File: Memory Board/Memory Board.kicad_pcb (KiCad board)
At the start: 4 copper layers, 50.8 x 50.8 mm, 40 parts, among them IC1 W25Q01JVZEIQ, IC2 MCP2557FDT-H_MNY, J1 USB4056-03-A_REVA2, J2 Conn_01x04_Socket, J3 Conn_01x04_Socket, J4 Conn_01x04_Socket, SW1 SW_SPST, U1 STM32G473CBTx, U2 LD1117S33TR_SOT223, U3 LD1117S50TR_SOT223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

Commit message: Layout work
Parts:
- added J5: Conn_01x02_Socket, Connector_PinHeader_2.54mm:PinHeader_1x02_P2.54mm_Vertical, F.Cu at (27.4, 37.2)
- J4: value Conn_01x04_Socket -> Conn_01x02_Socket; footprint Connector_PinHeader_2.54mm:PinHeader_1x04_P2.54mm_Vertical -> Connector_PinHeader_2.54mm:PinHeader_1x02_P2.54mm_Vertical
- moved C1 39.5 mm to (80.2, 35.5)
- moved C6 39.5 mm to (77.9, 35.1)
- moved C7 39.5 mm to (80.2, 32.6)
- moved C5 39.5 mm to (79.1, 34.6)
- moved C8 39.5 mm to (78.9, 32.1)
- moved D1 33.4 mm to (60.4, 53.0), turned to 180 degrees
- moved R2 30.9 mm to (57.3, 53.0), turned to 0 degrees
- moved C10 20.5 mm to (31.9, 49.7), turned to 90 degrees
- moved R3 19.8 mm to (39.5, 39.0), turned to -135 degrees
- moved R4 18.9 mm to (40.6, 40.1), turned to -135 degrees
- moved U2 18.1 mm to (37.1, 51.9), turned to 180 degrees
- moved R7 18.0 mm to (41.7, 41.2), turned to 45 degrees
- moved C11 17.5 mm to (44.4, 53.5), turned to 0 degrees
- moved C2 17.2 mm to (44.3, 41.7), turned to 90 degrees
- moved J1 17.1 mm to (49.5, 61.6)
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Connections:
- J4 pad 1: SYS_SWDIO -> SYS_SWCLK
- J4 pad 2: GND -> SYS_SWDIO
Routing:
- net GND: track 7.65 -> 22.8 mm, vias 4 -> 18
- net PWR IN: track 0.00 -> 7.37 mm
- net +5V: track 0.00 -> 6.94 mm
- net +3.3V: track 4.29 -> 9.08 mm, vias 1 -> 7
- net RCC_OCC_IN: track 0.00 -> 4.78 mm
- net SYS_SWCLK: track 0.00 -> 3.91 mm
- net SYS_SWDIO: track 0.00 -> 3.66 mm
- net RCC_OCC_OUT: track 0.00 -> 2.98 mm
- net Net-(D1-A): track 0.00 -> 1.46 mm
- added copper zone on F.Cu, net +3.3V
- added copper zone on F.Cu, net +5V
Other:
- board size 50.8 x 50.8 mm -> 38.1 x 38.1 mm
- board text added: "+3.3V"
- board text added: "3.3V REG"
- board text added: "5V REG"
- board text added: "CLK"
- board text added: "DIO"
- board text added: "GND"
- board text added: "PWR IN"
- board text added: "PWR ON"

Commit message: Lab Work
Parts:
- removed C11: .1uF, Capacitor_SMD:C_0402_1005Metric
- removed C12: 10uF, Capacitor_SMD:C_0603_1608Metric
- removed J5: Conn_01x02_Socket, Connector_PinHeader_2.54mm:PinHeader_1x02_P2.54mm_Vertical
- removed U3: LD1117S50TR_SOT223, Package_TO_SOT_SMD:SOT-223-3_TabPin2
- J4: value Conn_01x02_Socket -> Conn_01x04_Socket; footprint Connector_PinHeader_2.54mm:PinHeader_1x02_P2.54mm_Vertical -> Connector_PinHeader_2.54mm:PinHeader_1x04_P2.54mm_Vertical
- R3, R4, R7: footprint Resistor_SMD:R_0603_1608Metric -> Resistor_SMD:R_0402_1005Metric
- U1: moved to B.Cu
- moved C7 41.2 mm to (40.3, 43.4)
- moved C1 41.1 mm to (40.3, 45.8)
- moved C5 41.1 mm to (39.3, 44.9)
- moved C6 41.1 mm to (38.0, 45.4)
- moved C8 41.1 mm to (39.1, 42.4)
- moved D1 33.9 mm to (30.7, 36.5)
- moved R2 33.9 mm to (27.7, 36.5)
- moved J3 25.0 mm to (43.1, 62.0), turned to -90 degrees
- moved LED1 25.0 mm to (58.7, 51.0)
- moved C10 19.8 mm to (51.6, 47.6)
- moved IC2 19.8 mm to (34.6, 41.8), turned to 180 degrees
- moved R3 19.3 mm to (53.9, 51.8), turned to 0 degrees
- moved J4 17.3 mm to (43.1, 59.1)
- moved R4 16.4 mm to (53.9, 49.8), turned to 0 degrees
- moved R7 15.5 mm to (53.9, 50.8), turned to 180 degrees
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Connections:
- C15 pad 1: +5V -> PWR IN
- IC2 pad 3: +5V -> PWR IN
- J4 pad 1: SYS_SWCLK -> SYS_SWDIO
- J4 pad 2: SYS_SWDIO -> SYS_SWCLK
- U1 pad 25: unconnected-(U1-PB11-Pad25) -> LED_R
- U1 pad 27: unconnected-(U1-PB13-Pad27) -> LED_B
- U1 pad 29: unconnected-(U1-PB15-Pad29) -> LED_G
- U1 pad 30: LED_R -> unconnected-(U1-PA8-Pad30)
- U1 pad 31: LED_G -> unconnected-(U1-PA9-Pad31)
- U1 pad 32: LED_B -> unconnected-(U1-PA10-Pad32)
- U1 pad 39: TXD -> unconnected-(U1-PA15-Pad39)
- U1 pad 41: unconnected-(U1-PB4-Pad41) -> TXD
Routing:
- net GND: track 22.8 -> 0.00 mm, vias 18 -> 0
- net CAN_FD_H: track 15.1 -> 0.00 mm, vias 1 -> 0
- net CAN_FD_L: track 14.5 -> 0.00 mm, vias 2 -> 0
- net +3.3V: track 9.08 -> 0.00 mm, vias 7 -> 0
- net PWR IN: track 7.37 -> 0.00 mm
- net +5V: track 6.94 -> 0.00 mm
- net RCC_OCC_IN: track 4.78 -> 0.00 mm
- net SYS_SWCLK: track 3.91 -> 0.00 mm
- net SYS_SWDIO: track 3.66 -> 0.00 mm
- net Net-(C16-Pad2): track 3.28 -> 0.00 mm
- net RCC_OCC_OUT: track 2.98 -> 0.00 mm
- net Net-(SW1-B): track 2.22 -> 0.00 mm, vias 1 -> 0
- net Net-(D1-A): track 1.46 -> 0.00 mm
- removed copper zone on F.Cu, net +5V
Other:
- board text removed: "+3.3V"
- board text removed: "5V REG"
- board text removed: "GND"
- board text removed: "PWR IN"

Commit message: No work donw
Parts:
- moved C14 1.96 mm to (46.6, 37.4), turned to 0 degrees
- moved C13 1.86 mm to (44.7, 37.4), turned to 180 degrees
- moved D1 1.14 mm to (31.9, 36.6)
- moved R2 1.14 mm to (28.8, 36.6)
- moved X1 0.13 mm to (45.7, 35.4), turned to 90 degrees
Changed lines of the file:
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@@
   (net 64 "unconnected-(U1-PA10-Pad32)")
   (footprint "Capacitor_SMD:C_0402_1005Metric" (layer "F.Cu")
-    (at 46.546 37.3844)
+    (at 44.69 37.35 180)
     (descr "Capacitor SMD 0402 (1005 Metric), square (rectangular) end terminal, IPC_7351 nominal, (Body size source: IPC-SM-782 page 76, https://www.pcb-3d.com/wordpress/wp-content/uploads/ipc-sm-782a_amendment_1_and_2.pdf), generated with kicad-footprint-generator")
     (tags "capacitor")
@@
     (property "ki_keywords" "cap capacitor")
     (attr smd)
-    (fp_text reference "C13" (at 1.3522 -0.7942) (layer "F.SilkS")
+    (fp_text reference "C13" (at 1.46 0.82) (layer "F.SilkS")
         (effects (font (size 0.5 0.5) (thickness 0.1) bold))
     )
@@
     (fp_line (start 0.5 0.25) (end -0.5 0.25)
       (stroke (width 0.1) (type solid)) (layer "F.Fab"))
-    (pad "1" smd roundrect (at -0.48 0) (size 0.56 0.62) (layers "F.Cu" "F.Paste" "F.Mask") (roundrect_rratio 0.25)
+    (pad "1" smd roundrect (at -0.48 0 180) (size 0.56 0.62) (layers "F.Cu" "F.Paste" "F.Mask") (roundrect_rratio 0.25)
       (net 4 "RCC_OCC_IN") (pintype "passive"))
-    (pad "2" smd roundrect (at 0.48 0) (size 0.56 0.62) (layers "F.Cu" "F.Paste" "F.Mask") (roundrect_rratio 0.25)
+    (pad "2" smd roundrect (at 0.48 0 180) (size 0.56 0.62) (layers "F.Cu" "F.Paste" "F.Mask") (roundrect_rratio 0.25)
       (net 2 "GND") (pintype "passive"))
     (model "${KICAD6_3DMODEL_DIR}/Capacitor_SMD.3dshapes/C_0402_1005Metric.wrl"
@@
     (property "ki_keywords" "cap capacitor")
     (attr smd)
-    (fp_text reference "C2" (at 0 0 90) (layer "F.SilkS")
+    (fp_text reference "C2" (at 0.01 0.02 90) (layer "F.SilkS")
         (effects (font (size 0.25 0.25) (thickness 0.05) bold))
     )
@@
   )
   (footprint "Oscillator:Oscillator_SMD_ECS_2520MV-xxx-xx-4Pin_2.5x2.0mm" (layer "F.Cu")
-    (at 45.54 35.47 -90)
+    (at 45.66 35.42 90)
     (descr "Miniature Crystal Clock Oscillator ECS 2520MV series, https://www.ecsxtal.com/store/pdf/ECS-2520MV.pdf")
     (tags "Miniature Crystal Clock Oscillator ECS 2520MV series SMD SMT HCMOS")
@@
     (property "ki_keywords" "Crystal Clock Oscillator ECS SMD")
     (attr smd)
-    (fp_text reference "X1" (at -0.684999 -2.725) (layer "F.SilkS")
+    (fp_text reference "X1" (at 0.79 -2.53) (layer "F.SilkS")
         (effects (font (size 1 1) (thickness 0.15)))
     )
@@
     (fp_line (start 1 -1.25) (end 1 1.25)
       (stroke (width 0.1) (type solid)) (layer "F.Fab"))
-    (pad "1" smd roundrect (at -0.725 -0.925 270) (size 0.8 0.9) (layers "F.Cu" "F.Paste" "F.Mask") (roundrect_rratio 0.25)
+    (pad "1" smd roundrect (at -0.725 -0.925 90) (size 0.8 0.9) (layers "F.Cu" "F.Paste" "F.Mask") (roundrect_rratio 0.25)
       (net 4 "RCC_OCC_IN") (pinfunction "Tri-State") (pintype "input"))
-    (pad "2" smd roundrect (at -0.725 0.925 270) (size 0.8 0.9) (layers "F.Cu" "F.Paste" "F.Mask") (roundrect_rratio 0.25)
+    (pad "2" smd roundrect (at -0.725 0.925 90) (size 0.8 0.9) (layers "F.Cu" "F.Paste" "F.Mask") (roundrect_rratio 0.25)
       (net 2 "GND") (pinfunction "GND") (pintype "power_in"))
-    (pad "3" smd roundrect (at 0.725 0.925 270) (size 0.8 0.9) (layers "F.Cu" "F.Paste" "F.Mask") (roundrect_rratio 0.25)
+    (pad "3" smd roundrect (at 0.725 0.925 90) (size 0.8 0.9) (layers "F.Cu" "F.Paste" "F.Mask") (roundrect_rratio 0.25)
       (net 5 "RCC_OCC_OUT") (pinfunction "OUT") (pintype "output"))
-    (pad "4" smd roundrect (at 0.725 -0.925 270) (size 0.8 0.9) (layers "F.Cu" "F.Paste" "F.Mask") (roundrect_rratio 0.25)
+    (pad "4" smd roundrect (at 0.725 -0.925 90) (size 0.8 0.9) (layers "F.Cu" "F.Paste" "F.Mask") (roundrect_rratio 0.25)
       (net 2 "GND") (pinfunction "VDD") (pintype "power_in"))
     (model "${KICAD6_3DMODEL_DIR}/Oscillator.3dshapes/Oscillator_SMD_ECS_2520MV-xxx-xx-4Pin_2.5x2.0mm.wrl"
@@
   )
   (footprint "Capacitor_SMD:C_0402_1005Metric" (layer "F.Cu")
-    (at 44.6156 37.384401 180)
+    (at 46.58 37.35)
     (descr "Capacitor SMD 0402 (1005 Metric), square (rectangular) end terminal, IPC_7351 nominal, (Body size source: IPC-SM-782 page 76, https://www.pcb-3d.com/wordpress/wp-content/uploads/ipc-sm-782a_amendment_1_and_2.pdf), generated with kicad-footprint-generator")
     (tags "capacitor")
@@
     (property "ki_keywords" "cap capacitor")
     (attr smd)
-    (fp_text reference "C14" (at 1.5374 0.8142) (layer "F.SilkS")
+    (fp_text reference "C14" (at 1.47 -0.83) (layer "F.SilkS")
         (effects (font (size 0.5 0.5) (thickness 0.1) bold))
     )
@@
     (fp_line (start 0.5 0.25) (end -0.5 0.25)
       (stroke (width 0.1) (type solid)) (layer "F.Fab"))
-    (pad "1" smd roundrect (at -0.48 0 180) (size 0.56 0.62) (layers "F.Cu" "F.Paste" "F.Mask") (roundrect_rratio 0.25)
+    (pad "1" smd roundrect (at -0.48 0) (size 0.56 0.62) (layers "F.Cu" "F.Paste" "F.Mask") (roundrect_rratio 0.25)
       (net 5 "RCC_OCC_OUT") (pintype "passive"))
-    (pad "2" smd roundrect (at 0.48 0 180) (size 0.56 0.62) (layers "F.Cu" "F.Paste" "F.Mask") (roundrect_rratio 0.25)
+    (pad "2" smd roundrect (at 0.48 0) (size 0.56 0.62) (layers "F.Cu" "F.Paste" "F.Mask") (roundrect_rratio 0.25)
       (net 2 "GND") (pintype "passive"))
     (model "${KICAD6_3DMODEL_DIR}/Capacitor_SMD.3dshapes/C_0402_1005Metric.wrl"
@@
   )
   (footprint "LED_SMD:LED_0603_1608Metric" (layer "F.Cu")
-    (at 30.743401 36.55 180)
+    (at 31.878401 36.63 180)
     (descr "LED SMD 0603 (1608 Metric), square (rectangular) end terminal, IPC_7351 nominal, (Body size source: http://www.tortai-tech.com/upload/download/2011102023233369053.pdf), generated with kicad-footprint-generator")
     (tags "LED")
@@
   )
   (footprint "Resistor_SMD:R_0603_1608Metric" (layer "F.Cu")
-    (at 27.67 36.55)
+    (at 28.805 36.63)
     (descr "Resistor SMD 0603 (1608 Metric), square (rectangular) end terminal, IPC_7351 nominal, (Body size source: IPC-SM-782 page 72, https://www.pcb-3d.com/wordpress/wp-content/uploads/ipc-sm-782a_amendment_1_and_2.pdf), generated with kicad-footprint-generator")
     (tags "resistor")
@@
     (effects (font (size 0.5 0.5) (thickness 0.1)))
   )
-  (gr_text "PWR ON" (at 25.1359 35.7046) (layer "F.SilkS")
+  (gr_text "PWR ON" (at 26.2709 35.7846) (layer "F.SilkS")
     (effects (font (size 1.25 1.25) (thickness 0.25) bold) (justify left bottom))
   )

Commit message: Complete board
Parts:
- removed H3, H4: MountingHole_Pad, MountingHole:MountingHole_3.2mm_M3_Pad_TopBottom
- added G***: LOGO, LOGO, F.Cu at (37.9, 34.6)
- added G***: LOGO, LOGO, B.Cu at (50.4, 51.0)
- J1: footprint USB4056-03-A:GCT_USB4056-03-A_REVA2 -> Connector_USB:USB_C_Receptacle_GCT_USB4115-03-C
- RGB :): renamed from LED1
- moved H2 39.5 mm to (30.5, 58.4)
- moved R6 32.8 mm to (28.5, 41.0), turned to 90 degrees
- moved C16 30.3 mm to (30.0, 41.7), turned to -90 degrees
- moved SW1 29.8 mm to (31.5, 41.0), turned to 90 degrees
- moved R5 29.6 mm to (31.5, 40.9), turned to -90 degrees
- moved C10 21.6 mm to (30.2, 44.7), turned to 180 degrees
- moved RGB :) 17.0 mm to (41.8, 49.2), turned to 0 degrees
- moved C6 16.0 mm to (54.0, 43.5)
- moved C15 15.5 mm to (38.7, 38.9), turned to 90 degrees
- moved U2 14.1 mm to (32.3, 49.9), turned to 90 degrees
- moved C5 13.5 mm to (52.7, 43.0)
- moved C8 12.7 mm to (51.6, 40.0)
- moved C7 10.2 mm to (50.3, 41.0)
- moved R3 8.07 mm to (46.6, 48.4), turned to 180 degrees
- moved C1 7.98 mm to (42.3, 38.1), turned to -90 degrees
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- renumbered IC2 to CAN, IC1 to MEMES->
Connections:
- J2 pad 1: PWR IN -> GND
- J2 pad 2: PWR IN -> GND
- J2 pad 3: GND -> PWR IN
- J2 pad 4: GND -> PWR IN
- J3 pad 1: CAN_FD_L -> CAN_FD_H
- J3 pad 2: CAN_FD_L -> CAN_FD_H
- J3 pad 3: CAN_FD_H -> CAN_FD_L
- J3 pad 4: CAN_FD_H -> CAN_FD_L
- U1 pad 25: LED_R -> LED_G
- U1 pad 29: LED_G -> LED_R
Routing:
- net CAN_FD_L: track 0.00 -> 44.1 mm
- net PWR IN: track 0.00 -> 41.7 mm
- net GND: track 0.00 -> 34.9 mm, vias 0 -> 18
- net CAN_FD_H: track 0.00 -> 31.6 mm, vias 0 -> 1
- net QUADSPI_IO-0: track 0.00 -> 26.0 mm, vias 0 -> 1
- net +3.3V: track 0.00 -> 22.4 mm, vias 0 -> 12
- net QUADSPI_IO-3: track 0.00 -> 18.4 mm, vias 0 -> 1
- net SYS_SWCLK: track 0.00 -> 18.0 mm
- net SYS_SWDIO: track 0.00 -> 16.1 mm
- net QUADSPI_IO-1: track 0.00 -> 14.6 mm, vias 0 -> 1
- net QUADSPI_CLK: track 0.00 -> 14.4 mm, vias 0 -> 1
- net USB_D-: track 0.00 -> 14.2 mm, vias 0 -> 1
- net USB_D+: track 0.00 -> 14.2 mm, vias 0 -> 1
- net QUADSPI_IO-2: track 0.00 -> 13.7 mm, vias 0 -> 1
- net FDCAN_RX: track 0.00 -> 8.34 mm, vias 0 -> 1
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- added copper zone on F.Cu, net PWR IN
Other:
- board size 38.1 x 38.1 mm -> 29.8 x 38.1 mm
- board text added: "ALEX AARHUS"
- board text added: "BEEP BEEP BOOP BOOP"
- board text added: "CAN SWITCH"
- board text added: "GOOD MEMORIES"
- board text added: "SDSURP"
- board text removed: "CLK"
- board text removed: "DIO"

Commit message: Revisions
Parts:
- moved J4 7.61 mm to (35.5, 59.1), turned to 90 degrees
- moved C8 2.50 mm to (54.1, 39.9)
- moved C7 2.43 mm to (52.7, 41.0)
- moved C4 1.12 mm to (49.5, 42.6)
- moved C3 0.76 mm to (50.8, 43.1)
- moved C6 0.54 mm to (54.1, 43.0)
- moved C5 0.08 mm to (52.7, 43.0)
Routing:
- net SYS_SWDIO: track 16.1 -> 23.9 mm, vias 0 -> 1
- net GND: track 34.9 -> 37.9 mm, vias 18 -> 22
- net QUADSPI_IO-3: track 18.4 -> 16.7 mm
- net +3.3V: track 22.4 -> 21.8 mm

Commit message: Woek
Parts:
- added R8: 10k, Resistor_SMD:R_0402_1005Metric_Pad0.72x0.64mm_HandSolder, F.Cu at (40.5, 37.9)
- added SW2: SW_SPDT, Jumper:SolderJumper-3_P1.3mm_Open_RoundedPad1.0x1.5mm_NumberLabels, F.Cu at (40.3, 35.5)
- LED1: renamed from RGB :)
- SW1: footprint Jumper:SolderJumper-2_P1.3mm_Open_TrianglePad1.0x1.5mm -> Jumper:SolderJumper-2_P1.3mm_Open_RoundedPad1.0x1.5mm
- moved G*** 1.37 mm to (37.6, 33.3)
- moved D1 0.53 mm to (31.6, 36.2)
- moved R2 0.53 mm to (28.6, 36.2)
- renumbered MEMES-> to IC1, CAN to IC2
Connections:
- U1 pad 39: unconnected-(U1-PA15-Pad39) -> FDCAN_TX
- U1 pad 40: unconnected-(U1-PB3-Pad40) -> FDCAN_RX
- U1 pad 41: TXD -> unconnected-(U1-PB4-Pad41)
- U1 pad 42: unconnected-(U1-PB5-Pad42) -> TXD
- U1 pad 45: FDCAN_RX -> /BOOT0
- U1 pad 46: FDCAN_TX -> unconnected-(U1-PB9-Pad46)
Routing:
- net /BOOT0: track 0.00 -> 2.36 mm, vias 0 -> 1
- net FDCAN_RX: track 8.34 -> 10.6 mm
- net Net-(SW2-B): track 0.00 -> 1.97 mm
- net GND: track 37.9 -> 39.6 mm, vias 22 -> 23
- net +3.3V: track 21.8 -> 23.2 mm, vias 12 -> 13
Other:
- board text added: "CAN TERM RES"
- board text removed: "CAN SWITCH"

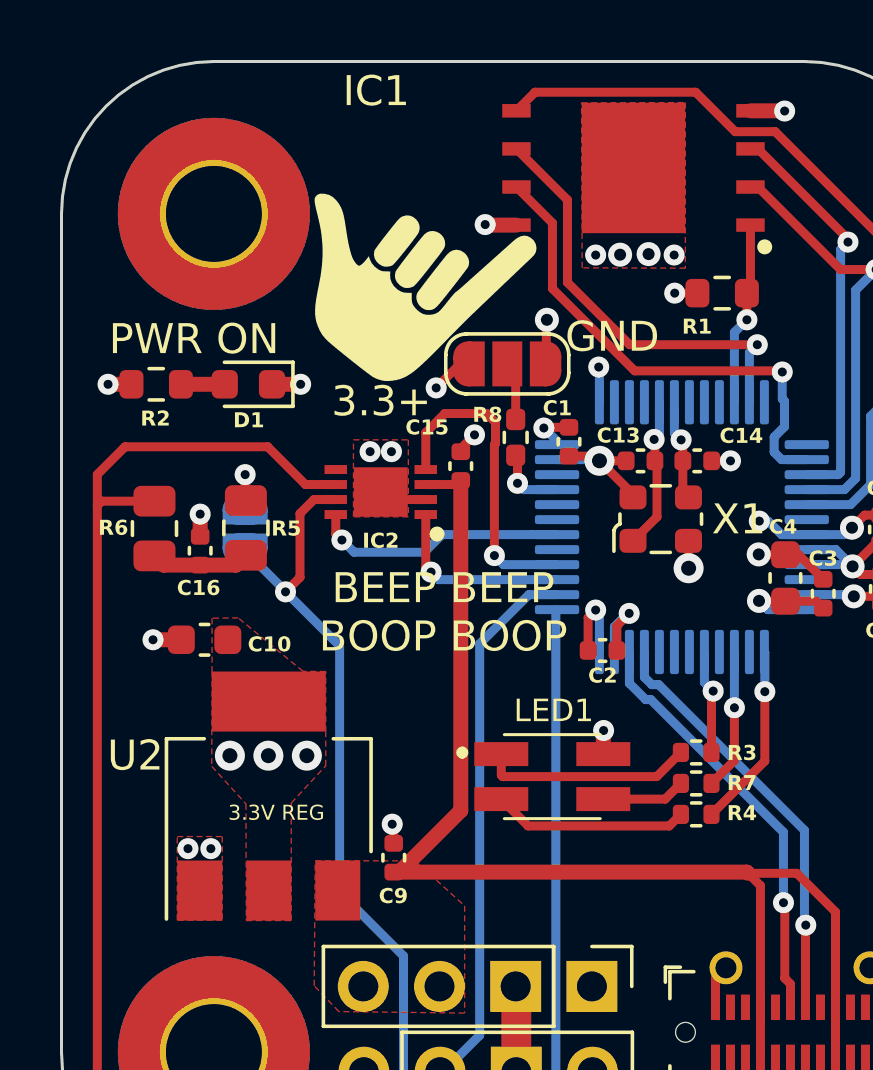
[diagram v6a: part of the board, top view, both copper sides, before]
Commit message: Added BOMS
https://www.digikey.com/short/8btm0n25
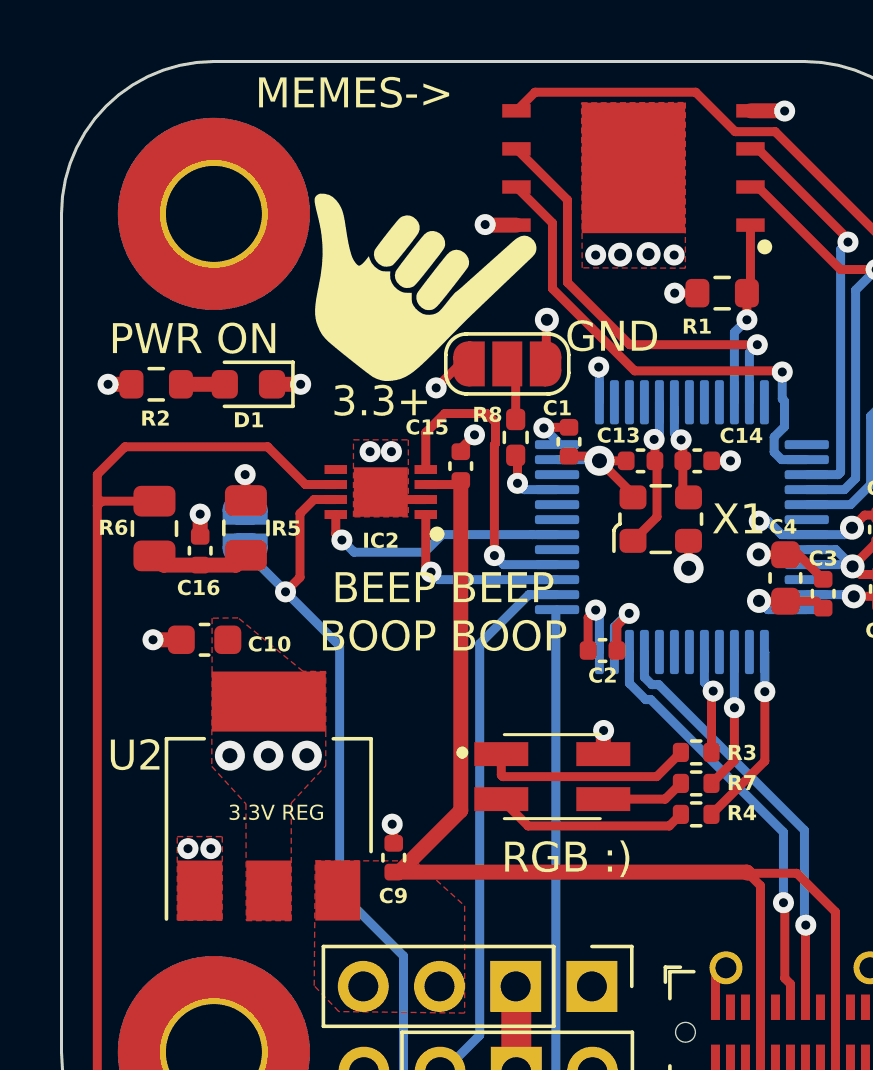
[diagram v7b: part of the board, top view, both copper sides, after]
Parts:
- renumbered IC1 to MEMES->
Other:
- board text added: "MEMES->"
- board text added: "RGB :)"
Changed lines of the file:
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@@
       (plot_on_all_layers_selection 0x0000000_00000000)
       (disableapertmacros false)
-      (usegerberextensions false)
-      (usegerberattributes true)
-      (usegerberadvancedattributes true)
-      (creategerberjobfile true)
+      (usegerberextensions true)
+      (usegerberattributes false)
+      (usegerberadvancedattributes false)
+      (creategerberjobfile false)
       (dashed_line_dash_ratio 12.000000)
       (dashed_line_gap_ratio 3.000000)
@@
       (psa4output false)
       (plotreference true)
-      (plotvalue true)
+      (plotvalue false)
       (plotinvisibletext false)
       (sketchpadsonfab false)
-      (subtractmaskfromsilk false)
+      (subtractmaskfromsilk true)
       (outputformat 1)
       (mirror false)
-      (drillshape 1)
+      (drillshape 0)
       (scaleselection 1)
-      (outputdirectory "")
+      (outputdirectory "Gerbs/")
     )
   )
@@
     (property "ki_description" "Standard LEDs - SMD RGB LED")
     (attr smd)
-    (fp_text reference "LED1" (at 0.049 -2.1964) (layer "F.SilkS")
+    (fp_text reference "LED1" (at 0.049 -2.1964) (layer "F.SilkS") hide
         (effects (font (size 0.75 0.75) (thickness 0.15)))
     )
@@
     (property "ki_description" "1G-bit Serial Flash Memory with uniform 4KB sectors and Dual/Quad SPI")
     (attr smd)
-    (fp_text reference "IC1" (at 8.575279 2.558036) (layer "F.SilkS")
+    (fp_text reference "MEMES->" (at 8.575279 2.558036) (layer "F.SilkS") hide
         (effects (font (size 1 1) (thickness 0.15)))
     )
@@
     (fp_line (start 1 0.625) (end -1 0.625)
       (stroke (width 0.1) (type solid)) (layer "F.Fab"))
-    (pad "1" smd roundrect (at -0.9125 0 90) (size 1.025 1.4) (layers "F.Cu" "F.Paste" "F.Mask") (roundrect_rratio 0.243902)
+    (pad "1" smd roundrect (at -0.9125 0 90) (size 1.025 1.4) (layers "F.Cu" "F.Paste" "F.Mask") (roundrect_rratio 0.243902439)
       (net 6 "Net-(C16-Pad2)") (pintype "passive"))
-    (pad "2" smd roundrect (at 0.9125 0 90) (size 1.025 1.4) (layers "F.Cu" "F.Paste" "F.Mask") (roundrect_rratio 0.243902)
+    (pad "2" smd roundrect (at 0.9125 0 90) (size 1.025 1.4) (layers "F.Cu" "F.Paste" "F.Mask") (roundrect_rratio 0.243902439)
       (net 30 "CAN_FD_L") (pintype "passive"))
     (model "${KICAD6_3DMODEL_DIR}/Resistor_SMD.3dshapes/R_0805_2012Metric.wrl"
@@
     (fp_line (start 1 0.625) (end -1 0.625)
       (stroke (width 0.1) (type solid)) (layer "F.Fab"))
-    (pad "1" smd roundrect (at -0.9125 0 270) (size 1.025 1.4) (layers "F.Cu" "F.Paste" "F.Mask") (roundrect_rratio 0.243902)
+    (pad "1" smd roundrect (at -0.9125 0 270) (size 1.025 1.4) (layers "F.Cu" "F.Paste" "F.Mask") (roundrect_rratio 0.243902439)
       (net 39 "Net-(SW1-B)") (pintype "passive"))
-    (pad "2" smd roundrect (at 0.9125 0 270) (size 1.025 1.4) (layers "F.Cu" "F.Paste" "F.Mask") (roundrect_rratio 0.243902)
+    (pad "2" smd roundrect (at 0.9125 0 270) (size 1.025 1.4) (layers "F.Cu" "F.Paste" "F.Mask") (roundrect_rratio 0.243902439)
       (net 6 "Net-(C16-Pad2)") (pintype "passive"))
     (model "${KICAD6_3DMODEL_DIR}/Resistor_SMD.3dshapes/R_0805_2012Metric.wrl"
@@
     (effects (font (size 0.5 0.5) (thickness 0.1)))
   )
+  (gr_text "MEMES->" (at 31.8516 27.051) (layer "F.SilkS")
+    (effects (font (size 1 1) (thickness 0.15)) (justify left bottom))
+  )
   (gr_text "PWR ON" (at 26.980399 35.2424) (layer "F.SilkS")
     (effects (font (size 1 1) (thickness 0.15)) (justify left bottom))
   )
+  (gr_text "RGB :)" (at 40.0558 52.5272) (layer "F.SilkS")
+    (effects (font (size 1 1) (thickness 0.15)) (justify left bottom))
+  )
